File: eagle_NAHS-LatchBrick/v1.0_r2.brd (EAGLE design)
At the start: 45.5 x 70.3 mm, 39 parts, among them IC1 ESP12F, IC2 ATTINY212-SSNR, IC3 TP4056, IC4 DW01A, IC5 FT232RL, J1 10118194-0001LF, Q1 8205A

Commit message: saving
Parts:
- removed C1, C3: 100nF, rcl:C0805
- removed IC5: FT232RL, ftdichip:SSOP28
- added J2: Brick-Interface, no_molex:500334-0160
- added R14: 10k, rcl:R0805
- moved TPB+ 8.74 mm to (38.7, 40.5)
- moved R11 8.64 mm to (31.1, 40.5)
- moved R12 8.64 mm to (35.4, 40.5)
- moved TPB- 8.64 mm to (27.8, 40.5)
- moved C5 6.87 mm to (32.0, 44.5)
- moved VR1 6.73 mm to (35.8, 44.5)
- moved IC2 6.48 mm to (36.8, 35.6)
- moved S1 6.48 mm to (36.8, 50.8)
- moved C4 5.68 mm to (39.4, 44.5), turned to 90 degrees
- moved R 5.08 mm to (42.0, 33.7)
- moved L2 1.27 mm to (24.6, 29.7)
- moved L1 1.27 mm to (29.7, 29.7)
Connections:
- removed net VCCIO: C3.1, IC5.17, IC5.4
- new net CD: IC3.8, J2.13, R14.2
- net +3V3: now also J2.16
- net D+: now also J2.9; no longer IC5.15
- net D-: now also J2.10; no longer IC5.16
- net IN+: now also J2.5, J2.6; no longer C1.1, IC5.20
- net IN-: now also J2.11, J2.12; no longer C1.2, C3.2, IC5.18, IC5.21, IC5.25, IC5.26, IC5.7
- net N$1: now also R14.1; no longer IC3.8
- net PROG: now also J2.1
- net RXD: now also J2.7; no longer IC5.1
- net SETUP: now also J2.2
- net TXD: now also J2.8; no longer IC5.5
- net UPDI: now also J2.15
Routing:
- net PROG: track 34.1 -> 92.7 mm, vias 1 -> 3
- net SETUP: track 50.8 -> 100.5 mm, vias 1 -> 3
- net +3V3: track 99.9 -> 149.0 mm, vias 1 -> 3
- net IN-: track 159.0 -> 118.9 mm, vias 4 -> 2
- net UPDI: track 34.3 -> 72.6 mm, vias 1 -> 3
- net IN+: track 65.5 -> 35.2 mm
- net VCCIO: track 23.3 -> 0.00 mm, vias 2 -> 0
- net CD: track 0.00 -> 8.69 mm
- net SCL: track 33.8 -> 41.6 mm
- net RST: track 78.1 -> 71.4 mm, vias 3 -> 2
- net SDA: track 34.5 -> 40.8 mm
- net SEL+: track 31.7 -> 25.5 mm
- net L2: track 16.1 -> 21.0 mm
- net L1: track 10.7 -> 14.1 mm
- net BAT-: track 13.9 -> 11.6 mm
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- added copper zone on layer 1, net IN-

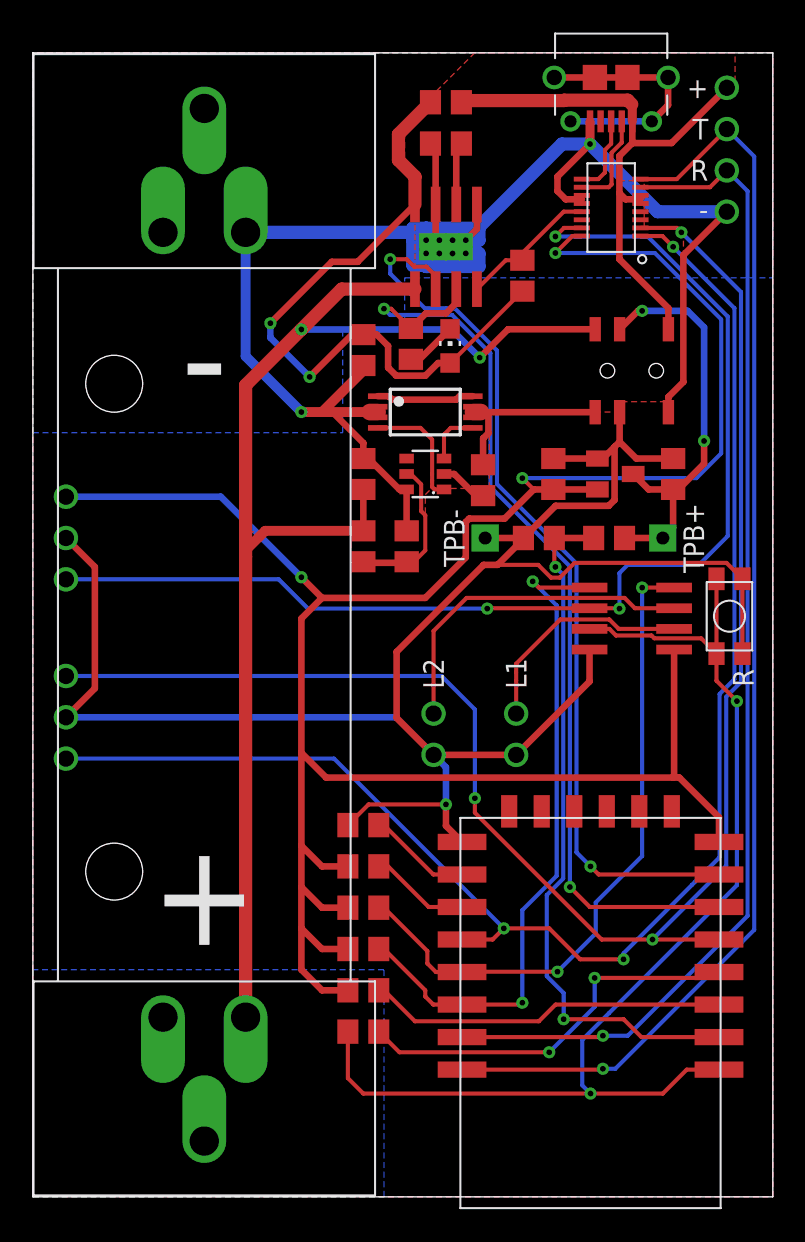
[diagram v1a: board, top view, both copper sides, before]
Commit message: komponenten mit kleineren bohrungen eingesetzt
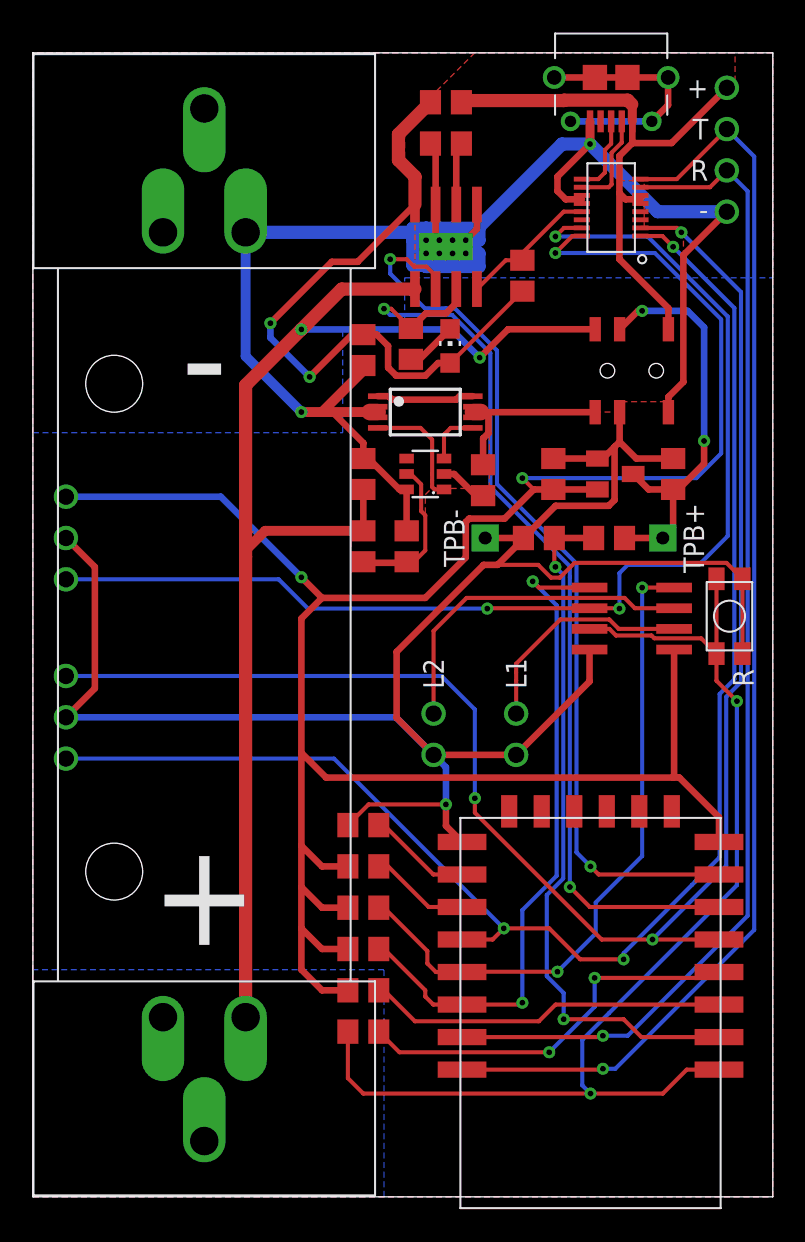
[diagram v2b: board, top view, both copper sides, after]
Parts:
- R11: value 590k -> 10k
- R12: value 2.7M -> 10k
- R13: value 1k -> 590k
- R14: value 10k -> 2.7M
- R5: value 1.74k -> 1k
- R6: value 3.9k -> 1.74k
- R8: value 10k -> 3.9k
- moved R5 54.8 mm to (20.3, 10.2), turned to 180 degrees
- moved R6 47.3 mm to (25.4, 64.8)
- moved R13 32.2 mm to (31.1, 40.5)
- moved R11 20.7 mm to (20.3, 22.9), turned to 0 degrees
- moved R12 17.0 mm to (30.1, 56.6), turned to 90 degrees
- moved R14 17.0 mm to (35.4, 40.5), turned to 180 degrees
- moved R9 7.62 mm to (20.3, 12.7)
- moved R7 2.54 mm to (20.3, 17.8)
- moved R8 2.54 mm to (20.3, 15.2)
- moved R10 2.54 mm to (20.3, 20.3)
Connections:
- net +3V3: now also R10.1; no longer R6.1
- net A0: now also R13.1, R14.2; no longer R11.1, R12.2
- net BOOT1: now also R10.2; no longer R9.2
- net BOOT2: now also R11.2; no longer R10.2
- net CD: now also R12.2; no longer R14.2
- net EN: now also R9.2; no longer R8.2
- net GND: now also R11.1, R13.2; no longer R10.1, R11.2
- net IN-: now also R6.1; no longer R5.1
- net N$1: now also R12.1; no longer R14.1
- net N$2: now also R6.2; no longer R5.2
- net RST: now also R5.2; no longer R13.2
- net SCL: now also R8.2; no longer R7.2
- net SDA: now also R7.2; no longer R6.2
- net SEL+: now also R14.1; no longer R12.1
- net WAKE: now also R5.1; no longer R13.1
